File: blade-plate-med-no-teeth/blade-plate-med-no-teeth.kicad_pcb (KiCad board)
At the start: 2 copper layers, 37.1 x 45.1 mm, 2 parts

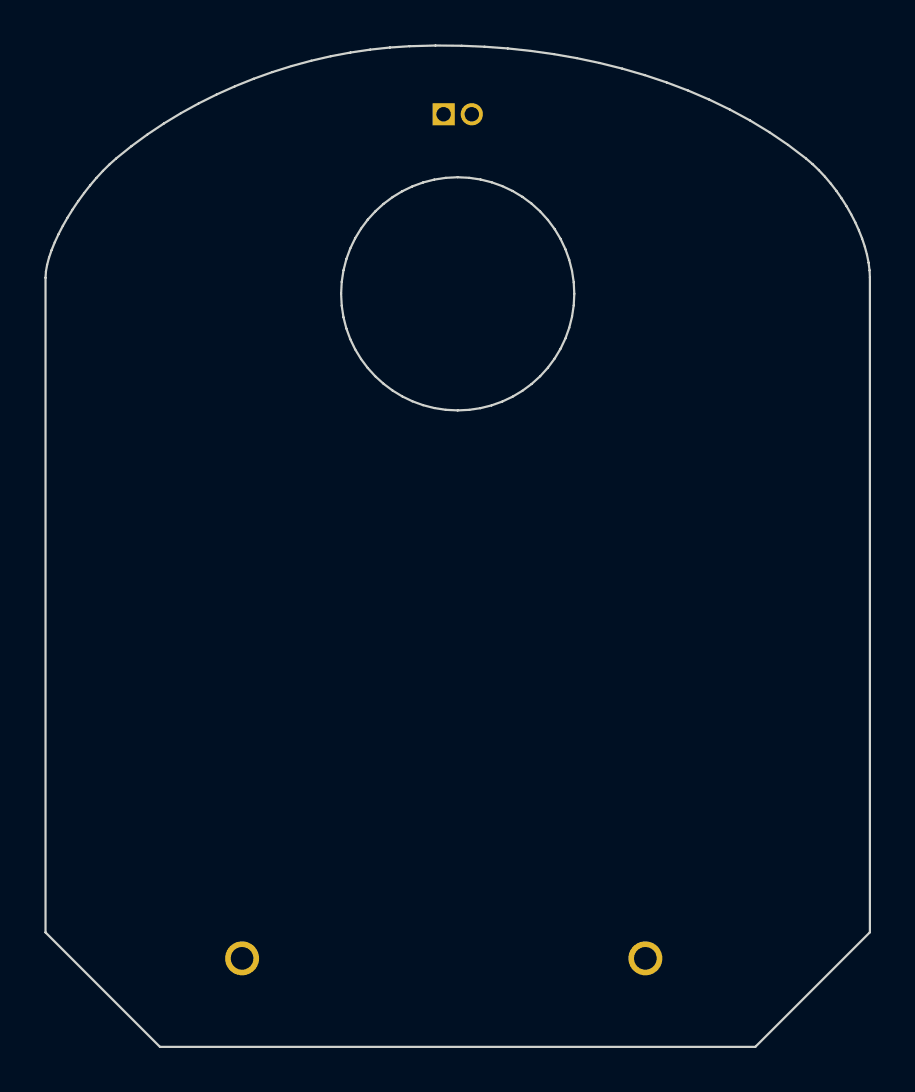
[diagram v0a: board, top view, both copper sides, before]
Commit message: Cleaned up SVGs Added art to blade-plate-med-no-teeth/blade-plate-med-no-teeth Updated art on Swadge-2021
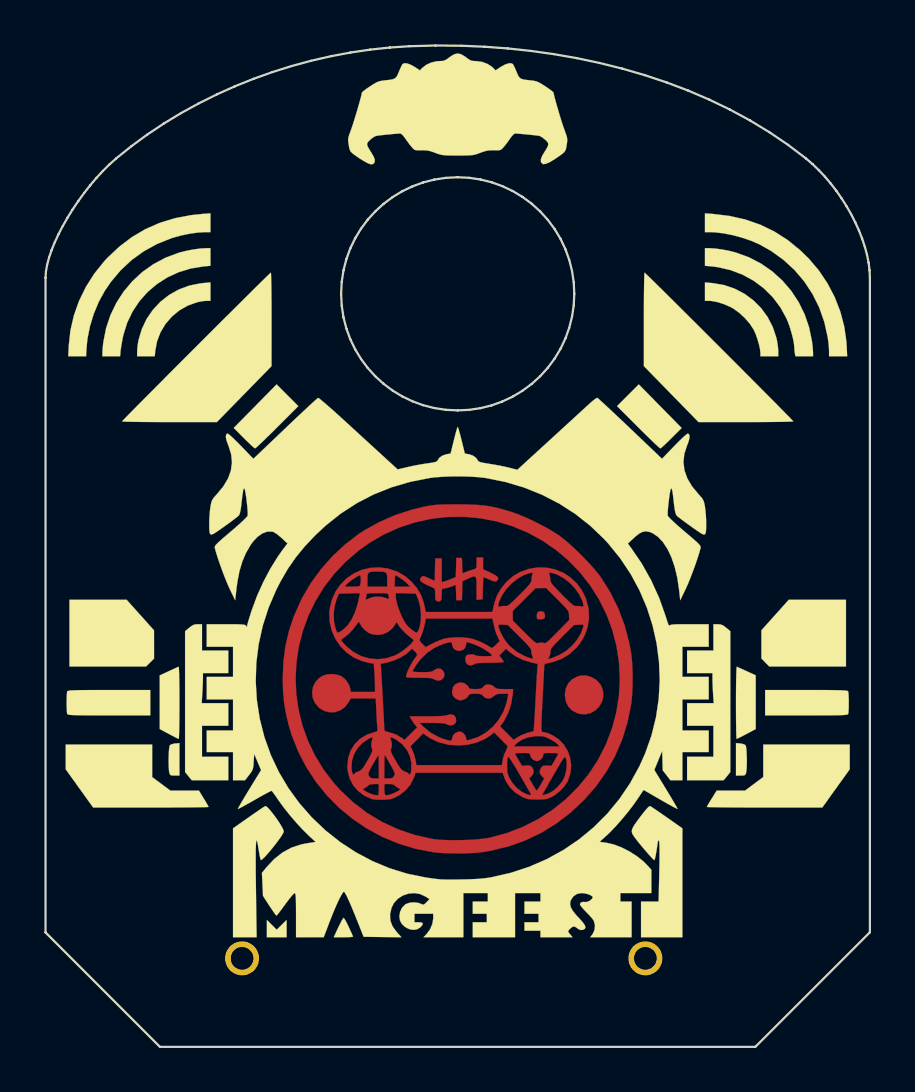
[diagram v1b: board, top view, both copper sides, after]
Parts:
- added Ref**: Val**, Swadge_Parts:guide-bar, F.Cu at (0.00, -2.29)

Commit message: Redid vector art for guide bar
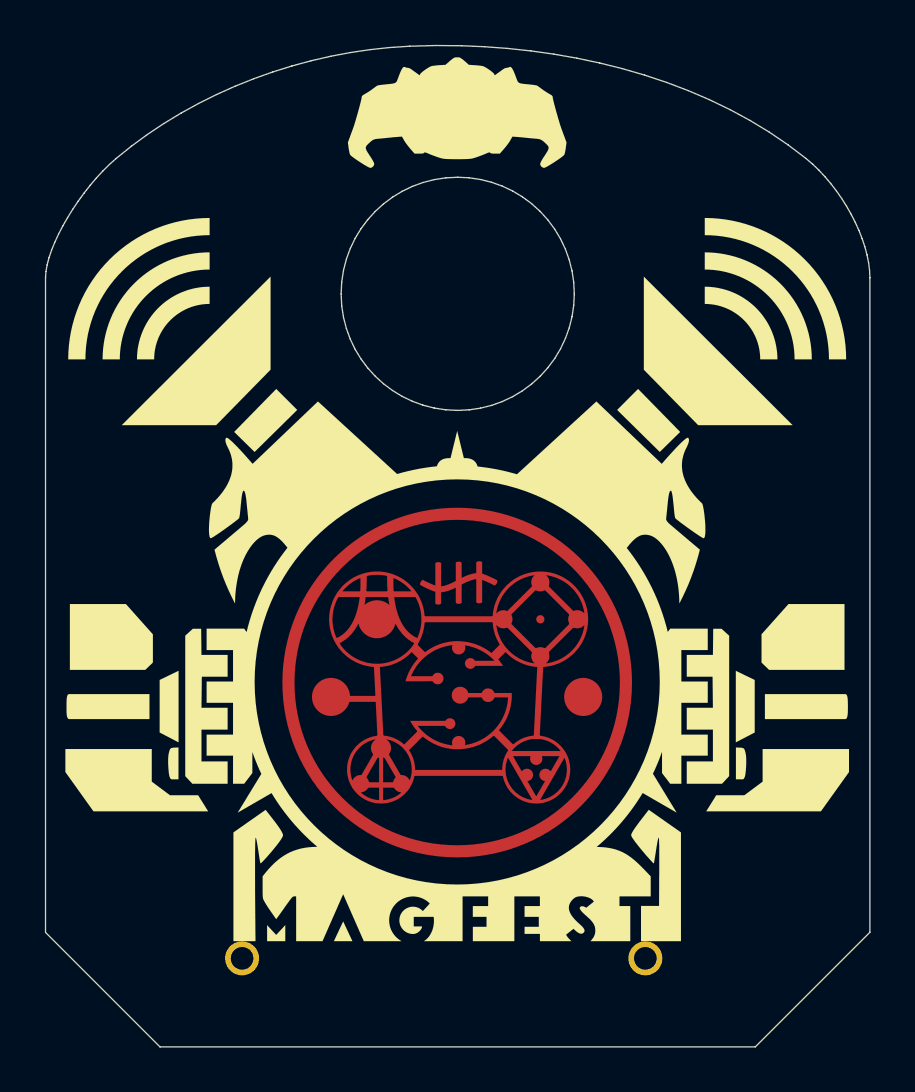
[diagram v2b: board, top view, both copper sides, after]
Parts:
- removed the Ref** at (0.00, -2.29)

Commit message: Added split art to guidebar
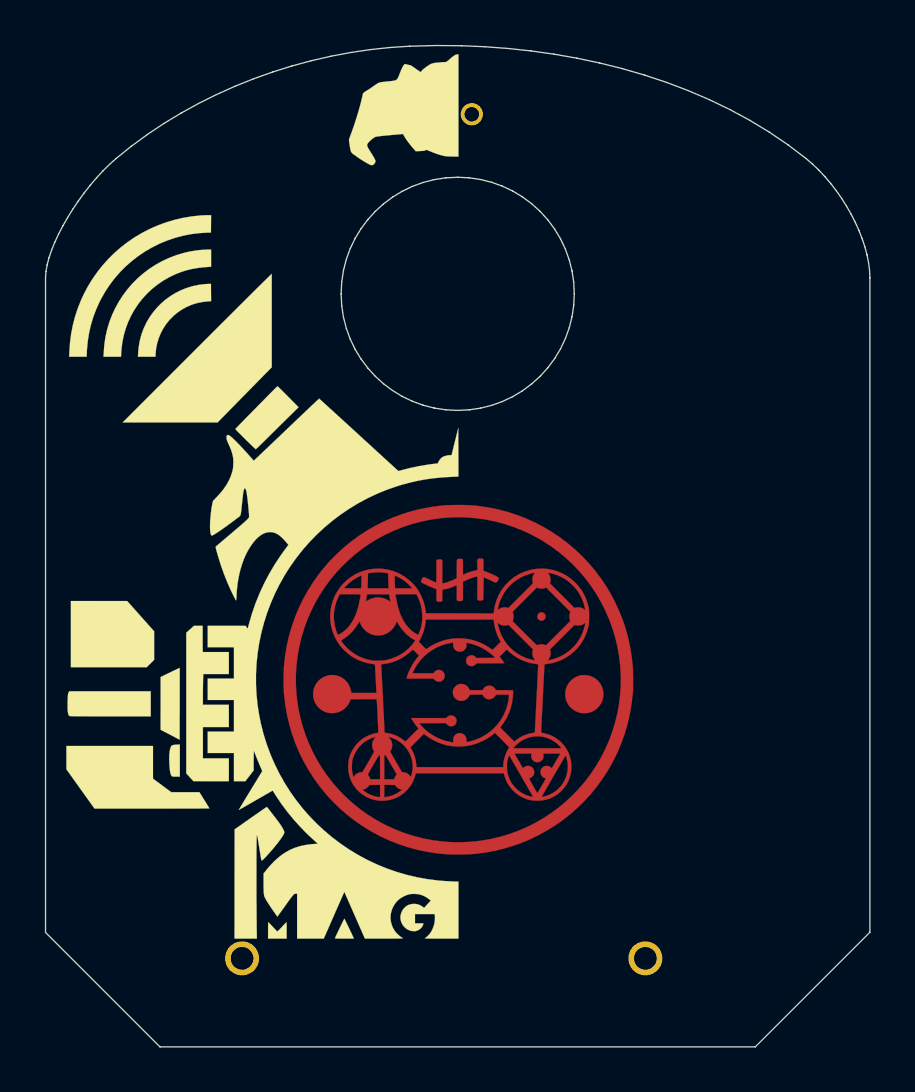
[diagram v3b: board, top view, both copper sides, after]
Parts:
- added Ref**: Val**, Swadge_Parts:test_guide_bar_holes, F.Cu at (0.02, 0.03)

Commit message: Updated guide bar with LED runes
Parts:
- removed the Ref** at (0.02, 0.03)
- added Ref**: Val**, Swadge_Parts:guide-bar, F.Cu at (0.00, 0.00)
